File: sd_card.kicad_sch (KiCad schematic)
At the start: 6 parts, among them J7 Micro_SD_Card_Det1

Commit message: mostly done except for RTL8305 power stuff
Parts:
- D6, D7, J7: now left out of the parts list
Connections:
- net SDMMC_CD: now also D7.4 (IO3); no longer D7.6 (IO4)
- net SDMMC_CLK: now also D7.3 (IO2); no longer D7.1 (IO1)
- net SDMMC_CMD: now also D6.6 (IO4); no longer D7.3 (IO2)
- net SDMMC_D0: now also D7.1 (IO1); no longer D6.1 (IO1)
- net SDMMC_D1: now also D7.6 (IO4); no longer D6.3 (IO2)
- net SDMMC_D2: now also D6.1 (IO1); no longer D6.6 (IO4)
- net SDMMC_D3: now also D6.3 (IO2); no longer D6.4 (IO3)
- net SDMMC_VDD: now also D6.5 (VCC); no longer D7.5 (VCC)
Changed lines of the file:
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@@
 	)
 	(label "SDMMC_CLK"
+		(at 189.23 96.52 180)
+		(effects
+			(font
+				(size 1.27 1.27)
+			)
+			(justify right bottom)
+		)
+	)
+	(label "SDMMC_CMD"
+		(at 205.74 62.23 0)
+		(effects
+			(font
+				(size 1.27 1.27)
+			)
+			(justify left bottom)
+		)
+	)
+	(label "SDMMC_D1"
+		(at 205.74 88.9 0)
+		(effects
+			(font
+				(size 1.27 1.27)
+			)
+			(justify left bottom)
+		)
+	)
+	(label "SDMMC_D0"
 		(at 189.23 88.9 180)
 		(effects
@@
 		)
 	)
-	(label "SDMMC_CMD"
-		(at 189.23 96.52 180)
+	(label "SDMMC_CD"
+		(at 205.74 96.52 0)
+		(effects
+			(font
+				(size 1.27 1.27)
+			)
+			(justify left bottom)
+		)
+	)
+	(label "SDMMC_D2"
+		(at 189.23 62.23 180)
 		(effects
 			(font
@@
 		)
 	)
-	(label "SDMMC_D1"
+	(label "SDMMC_VDD"
+		(at 205.74 66.04 0)
+		(effects
+			(font
+				(size 1.27 1.27)
+			)
+			(justify left bottom)
+		)
+	)
+	(label "SDMMC_D3"
 		(at 189.23 69.85 180)
 		(effects
@@
 			)
 			(justify right bottom)
-		)
-	)
-	(label "SDMMC_D0"
-		(at 189.23 62.23 180)
-		(effects
-			(font
-				(size 1.27 1.27)
-			)
-			(justify right bottom)
-		)
-	)
-	(label "SDMMC_CD"
-		(at 205.74 88.9 0)
-		(effects
-			(font
-				(size 1.27 1.27)
-			)
-			(justify left bottom)
-		)
-	)
-	(label "SDMMC_D2"
-		(at 205.74 62.23 0)
-		(effects
-			(font
-				(size 1.27 1.27)
-			)
-			(justify left bottom)
-		)
-	)
-	(label "SDMMC_VDD"
-		(at 205.74 92.71 0)
-		(effects
-			(font
-				(size 1.27 1.27)
-			)
-			(justify left bottom)
-		)
-	)
-	(label "SDMMC_D3"
-		(at 205.74 69.85 0)
-		(effects
-			(font
-				(size 1.27 1.27)
-			)
-			(justify left bottom)
 		)
 	)
@@
 		(unit 1)
 		(exclude_from_sim no)
-		(in_bom yes)
+		(in_bom no)
 		(on_board yes)
 		(dnp yes)
@@
 		(unit 1)
 		(exclude_from_sim no)
-		(in_bom yes)
+		(in_bom no)
 		(on_board yes)
 		(dnp yes)
@@
 		(unit 1)
 		(exclude_from_sim no)
-		(in_bom yes)
+		(in_bom no)
 		(on_board yes)
 		(dnp yes)

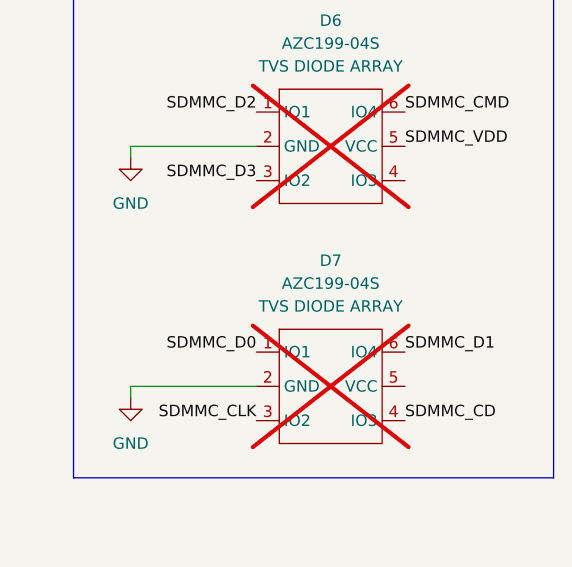
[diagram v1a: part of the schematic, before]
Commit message: replaced ferrites with 0 omh resitors, finalized standoff solution
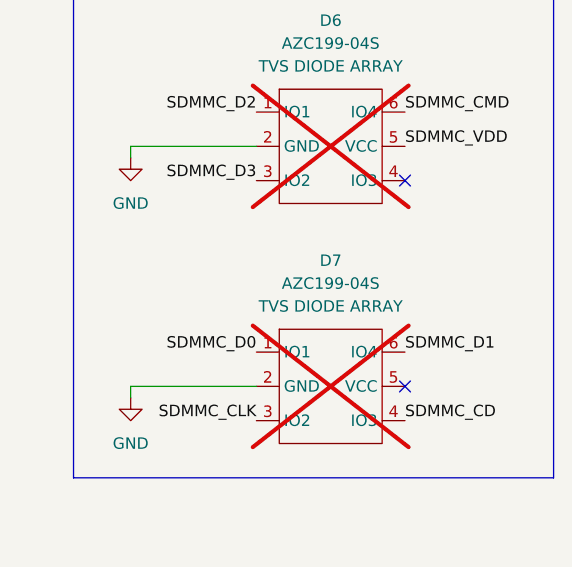
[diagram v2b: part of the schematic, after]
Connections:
- no-connect marks 0 -> 2
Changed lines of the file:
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@@
 		(color 0 0 0 0)
+	)
+	(no_connect
+		(at 205.74 92.71)
+	)
+	(no_connect
+		(at 205.74 69.85)
 	)
 	(wire

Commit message: finalized board for fabrication
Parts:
- C10: LCSC Part # (none) -> C15525
- C11: LCSC Part # (none) -> C96446
- R3: LCSC Part # (none) -> C25092
